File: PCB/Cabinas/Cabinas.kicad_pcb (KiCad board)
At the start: 2 copper layers, 196.7 x 93.5 mm, 116 parts, among them J1 JACK_ST_3SW, K1 CONN_3, M1 WTV020-SD, P1 CONN_2, P10 CONN_2, P11 CONN_2, P12 CONN_2, P13 DIN_5, P2 CONN_2, P3 CONN_2, P4 CONN_2, P5 CONN_2, P6 CONN_2, P7 CONN_2, P8 CONN_2, P9 CONN_2, Q1 MOSFET_N, Q10 MOSFET_N, Q11 MOSFET_N, Q12 MOSFET_N, Q2 MOSFET_N, Q3 MOSFET_N, Q4 MOSFET_N, Q5 MOSFET_N, Q6 MOSFET_N, Q7 MOSFET_N, Q8 MOSFET_N, Q9 MOSFET_N, SW1 PUSHBUTTON, SW10 PUSHBUTTON, SW11 PUSHBUTTON, SW12 PUSHBUTTON, SW2 PUSHBUTTON, SW3 PUSHBUTTON, SW4 PUSHBUTTON, SW5 PUSHBUTTON, SW6 PUSHBUTTON, SW7 PUSHBUTTON, SW8 PUSHBUTTON, SW9 PUSHBUTTON, U1 BTM, U2 7805, U3 TL072

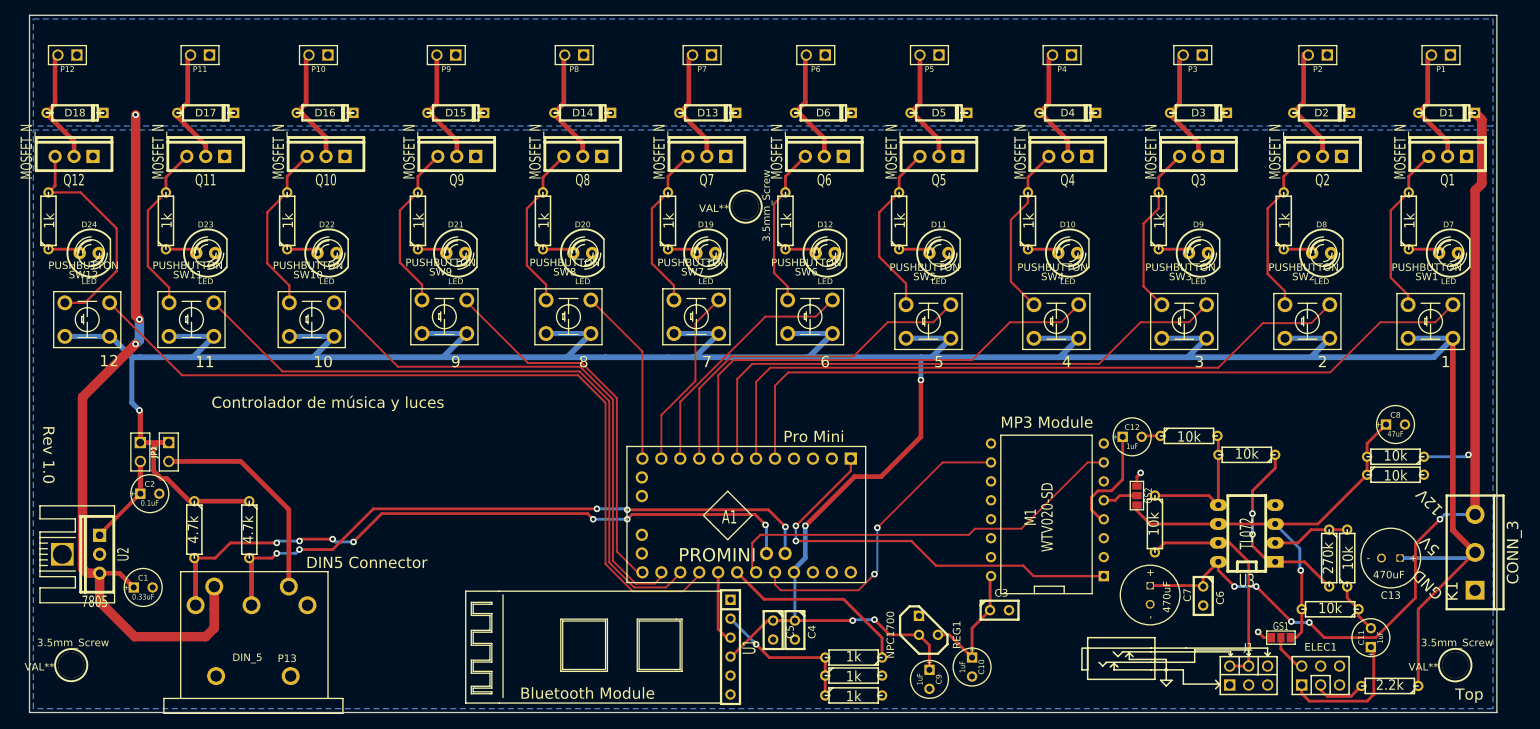
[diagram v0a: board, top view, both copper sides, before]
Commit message: Shift registers
Se añadieron shift registers
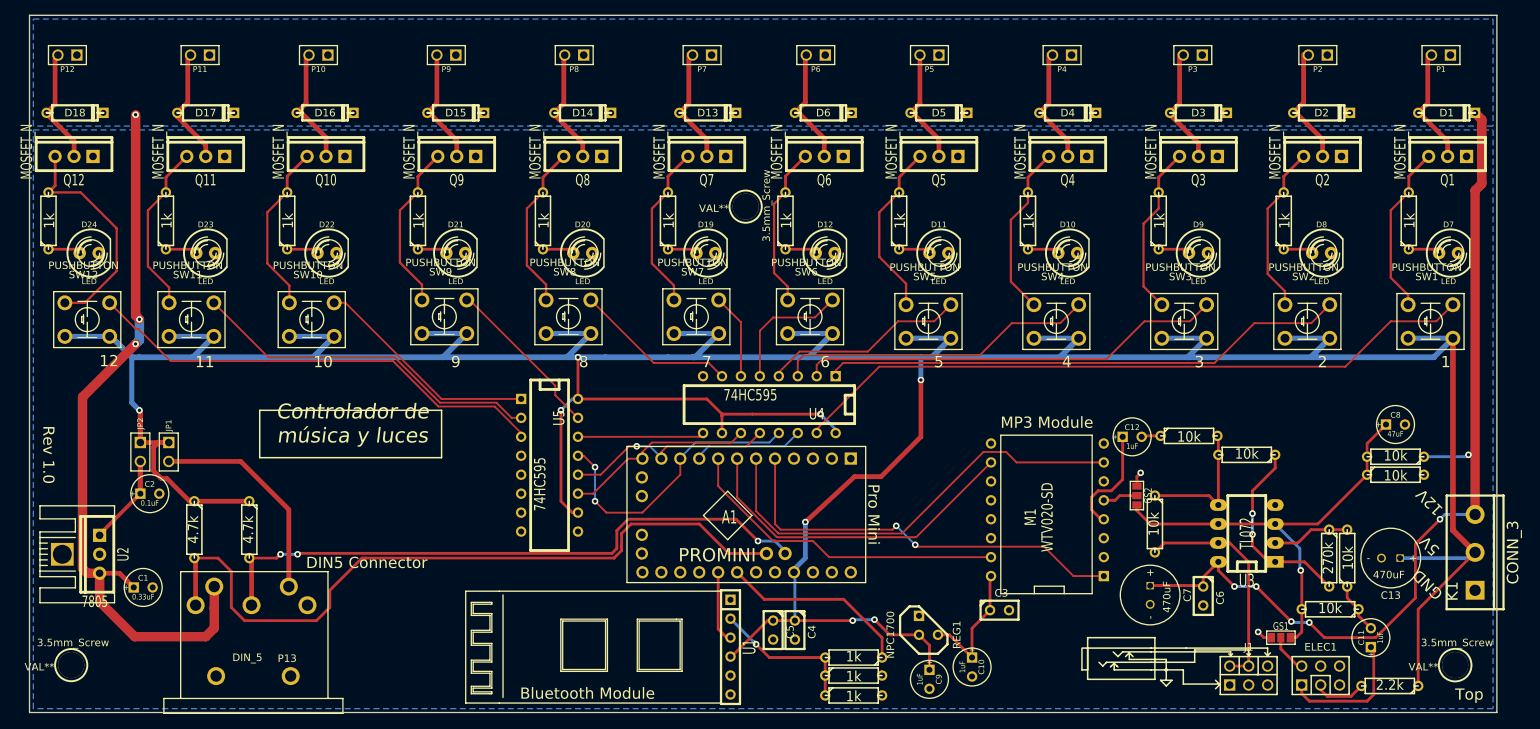
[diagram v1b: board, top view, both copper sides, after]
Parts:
- added U4: 74HC595, DIP-16__300, F.Cu at (139.2, 109.7)
- added U5: 74HC595, DIP-16__300, F.Cu at (109.7, 117.9)
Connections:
- A1 pad 1: MP3_RESET -> (no net)
- A1 pad 10: D7 -> SR_OE
- A1 pad 11: D8 -> SR_LCLK
- A1 pad 12: D9 -> SR_CLK
- A1 pad 17: D10 -> (no net)
- A1 pad 18: D11 -> (no net)
- A1 pad 19: D12 -> (no net)
- A1 pad 20: D13 -> (no net)
- A1 pad 23: MP3_CK -> (no net)
- A1 pad 24: MP3_DATA -> (no net)
- A1 pad 5: D2 -> MP3_RESET
- A1 pad 6: D3 -> MP3_CK
- A1 pad 7: D4 -> MP3_DATA
- A1 pad 8: D5 -> MP3_BUSY
- A1 pad 9: D6 -> SR_Input
- M1 pad 15: (no net) -> MP3_BUSY
- SW1 pad 2: D2 -> 1
- SW10 pad 2: D11 -> 10
- SW11 pad 2: D12 -> 11
- SW12 pad 2: D13 -> 12
- SW2 pad 2: D3 -> 2
- SW3 pad 2: D4 -> 3
- SW4 pad 2: D5 -> 4
- SW5 pad 2: D6 -> 5
- SW6 pad 2: D7 -> 6
- SW7 pad 2: D8 -> 7
- SW8 pad 2: D9 -> 8
- SW9 pad 2: D10 -> 9
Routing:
- net D13: track 109.0 -> 0.00 mm
- net D2: track 105.2 -> 0.00 mm
- net 1: track 0.00 -> 92.7 mm
- net D12: track 91.9 -> 0.00 mm
- net D3: track 91.5 -> 0.00 mm
- net D4: track 77.7 -> 0.00 mm
- net D11: track 73.1 -> 0.00 mm
- net 2: track 0.00 -> 70.7 mm
- net D5: track 63.4 -> 0.00 mm
- net +5V: track 470.6 -> 533.9 mm, vias 5 -> 8
- net 12: track 0.00 -> 62.9 mm
- net 3: track 0.00 -> 57.1 mm
- net D10: track 50.9 -> 0.00 mm
- net D6: track 47.8 -> 0.00 mm
- net 11: track 0.00 -> 47.6 mm
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
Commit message: Revision final
Revision final
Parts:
- removed C13: 470uF, CAP_8_3.5
- removed GS1, GS2: GS3, GS3
- removed U4, U5: 74HC595, DIP-16__300
- C7: footprint CAP_8_3.5 -> C1V5
- moved C6 2.67 mm to (194.7, 135.3)
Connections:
- A1 pad 10: SR_OE -> D7
- A1 pad 11: SR_LCLK -> D8
- A1 pad 12: SR_CLK -> D9
- A1 pad 15: (no net) -> MP3_CK
- A1 pad 16: (no net) -> MP3_RESET
- A1 pad 17: (no net) -> D10
- A1 pad 18: (no net) -> D11
- A1 pad 19: (no net) -> D12
- A1 pad 20: (no net) -> D13
- A1 pad 23: (no net) -> MP3_BUSY
- A1 pad 24: (no net) -> MP3_DATA
- A1 pad 5: MP3_RESET -> D2
- A1 pad 6: MP3_CK -> D3
- A1 pad 7: MP3_DATA -> D4
- A1 pad 8: MP3_BUSY -> D5
- A1 pad 9: SR_Input -> D6
- C3 pad 2: GND -> N-0000046
- C4 pad 2: GND -> N-0000046
- C5 pad 2: GND -> N-0000046
- C6 pad 2: GND -> N-0000046
- C7 pad 2: GND -> N-0000046
- ELEC1 pad 2: N-0000058 (its old number) -> Vbias
- M1 pad 5: N-0000062 (its old number) -> Vbias
- SW1 pad 2: 1 -> D2
- SW10 pad 2: 10 -> D11
- SW11 pad 2: 11 -> D12
- SW12 pad 2: 12 -> D13
- SW2 pad 2: 2 -> D3
- SW3 pad 2: 3 -> D4
- SW4 pad 2: 4 -> D5
- SW5 pad 2: 5 -> D6
- SW6 pad 2: 6 -> D7
- SW7 pad 2: 7 -> D8
- SW8 pad 2: 8 -> D9
- SW9 pad 2: 9 -> D10
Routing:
- net D13: track 0.00 -> 109.0 mm
- net D2: track 0.00 -> 105.2 mm
- net 1: track 92.7 -> 0.00 mm
- net D12: track 0.00 -> 91.9 mm
- net D3: track 0.00 -> 91.5 mm
- net D4: track 0.00 -> 77.7 mm
- net +5V: track 533.9 -> 460.2 mm, vias 8 -> 5
- net D11: track 0.00 -> 73.1 mm
- net 2: track 70.7 -> 0.00 mm
- net N-0000046: track 0.00 -> 69.9 mm
- net D5: track 0.00 -> 63.4 mm
- net 12: track 62.9 -> 0.00 mm
- net 3: track 57.1 -> 0.00 mm
- net D10: track 0.00 -> 50.9 mm
- net D6: track 0.00 -> 47.8 mm
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
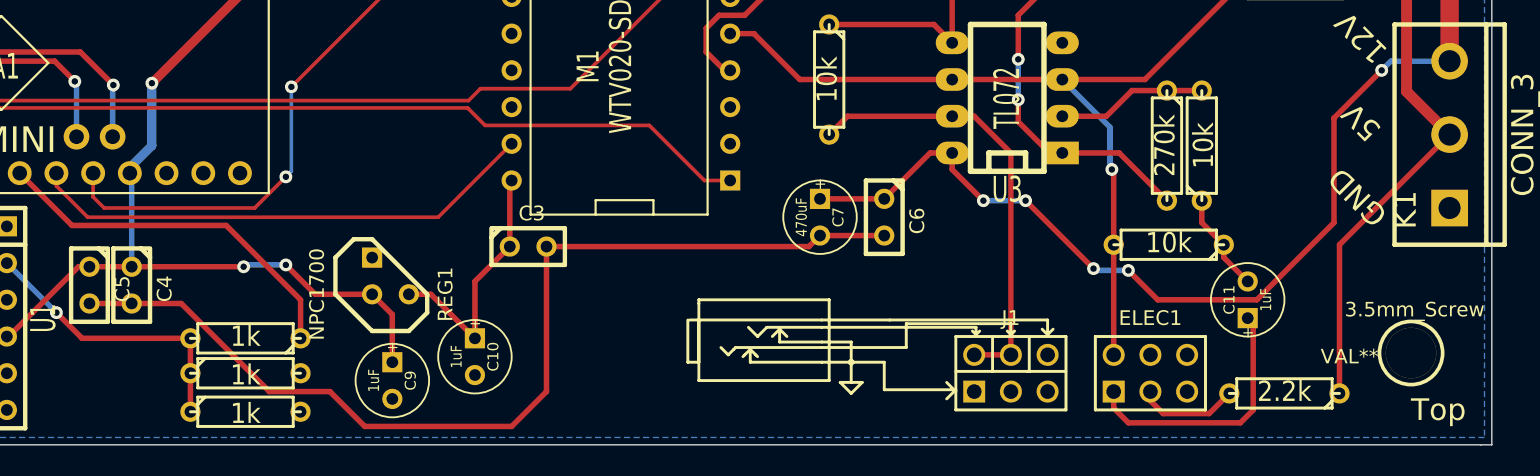
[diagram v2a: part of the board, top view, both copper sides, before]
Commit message: Cambios
Cambio en los capacitores de desacoplamiento y sus footprints.
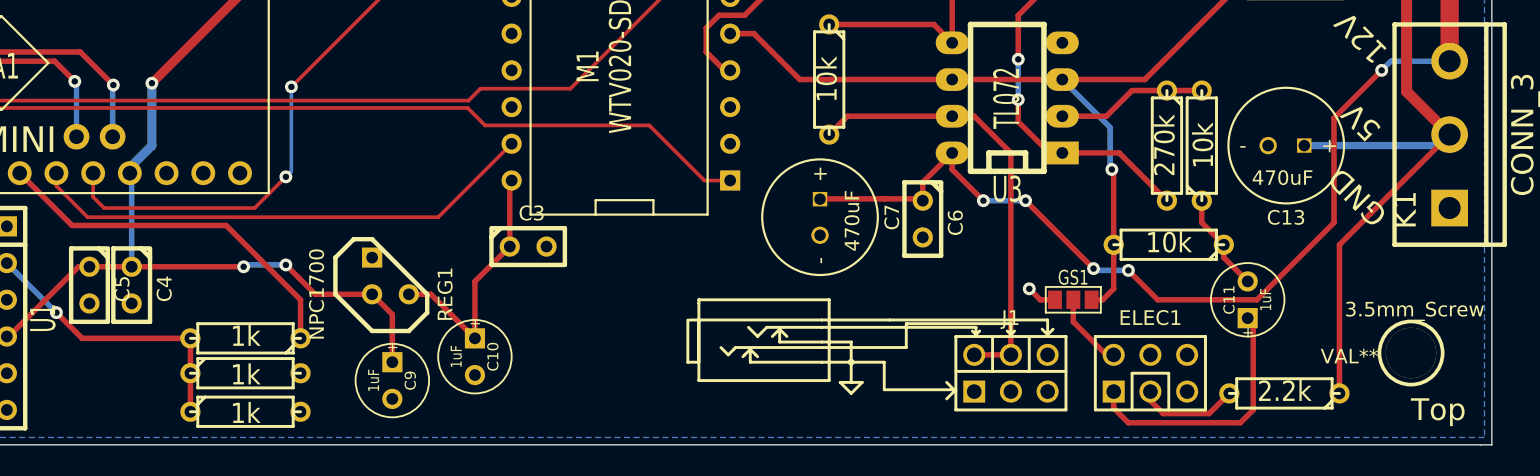
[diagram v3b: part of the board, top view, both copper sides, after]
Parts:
- added C13: 470uF, CAP_8_3.5, F.Cu at (222.5, 130.3)
- added GS1: GS3, GS3, F.Cu at (207.8, 141.0)
- C7: footprint C1V5 -> CAP_8_3.5
- moved C6 2.67 mm to (197.4, 135.4)
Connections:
- C3 pad 2: N-0000046 -> GND
- C4 pad 2: N-0000046 -> GND
- C5 pad 2: N-0000046 -> GND
- C6 pad 2: N-0000046 -> GND
- C7 pad 2: N-0000046 -> GND
- ELEC1 pad 2: Vbias -> N-0000046
- ELEC1 pad 4: (no net) -> GND
- ELEC1 pad 6: (no net) -> GND
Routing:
- net N-0000046: track 69.9 -> 5.26 mm
- net +5V: track 460.2 -> 470.6 mm
- net Vbias: track 67.7 -> 64.9 mm
- net GND: track 0.00 -> 2.09 mm, vias 0 -> 1
- net +12V: track 276.4 -> 277.3 mm

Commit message: Cambios
Cambio de pines para el módulo MP3
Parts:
- added GS2: GS3, GS3, F.Cu at (188.5, 121.9)
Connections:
- A1 pad 1: (no net) -> MP3_RESET
- A1 pad 15: MP3_CK -> (no net)
- A1 pad 16: MP3_RESET -> (no net)
- A1 pad 23: MP3_BUSY -> MP3_CK
- ELEC1 pad 4: GND -> (no net)
- ELEC1 pad 6: GND -> (no net)
- M1 pad 15: MP3_BUSY -> (no net)
- M1 pad 5: Vbias -> N-0000055
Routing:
- net MP3_BUSY: track 35.4 -> 0.00 mm
- net MP3_CK: track 65.9 -> 55.7 mm
- net MP3_RESET: track 64.8 -> 57.3 mm, vias 0 -> 2
- net N-0000055: track 0.00 -> 4.70 mm
- net Vbias: track 64.9 -> 60.7 mm
- net GND: track 2.09 -> 4.08 mm, vias 1 -> 2
